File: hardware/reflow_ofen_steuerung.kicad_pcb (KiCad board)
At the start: 2 copper layers, 150.9 x 55.9 mm, 49 parts, among them J1 230VAC, J10 GND, J2 Heizung oben, J3 Heizung unten, J4 AVR-ISP-6, J5 LCD Display, J6 Encoder, J7 FAN, J8 +5V, J9 +12V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

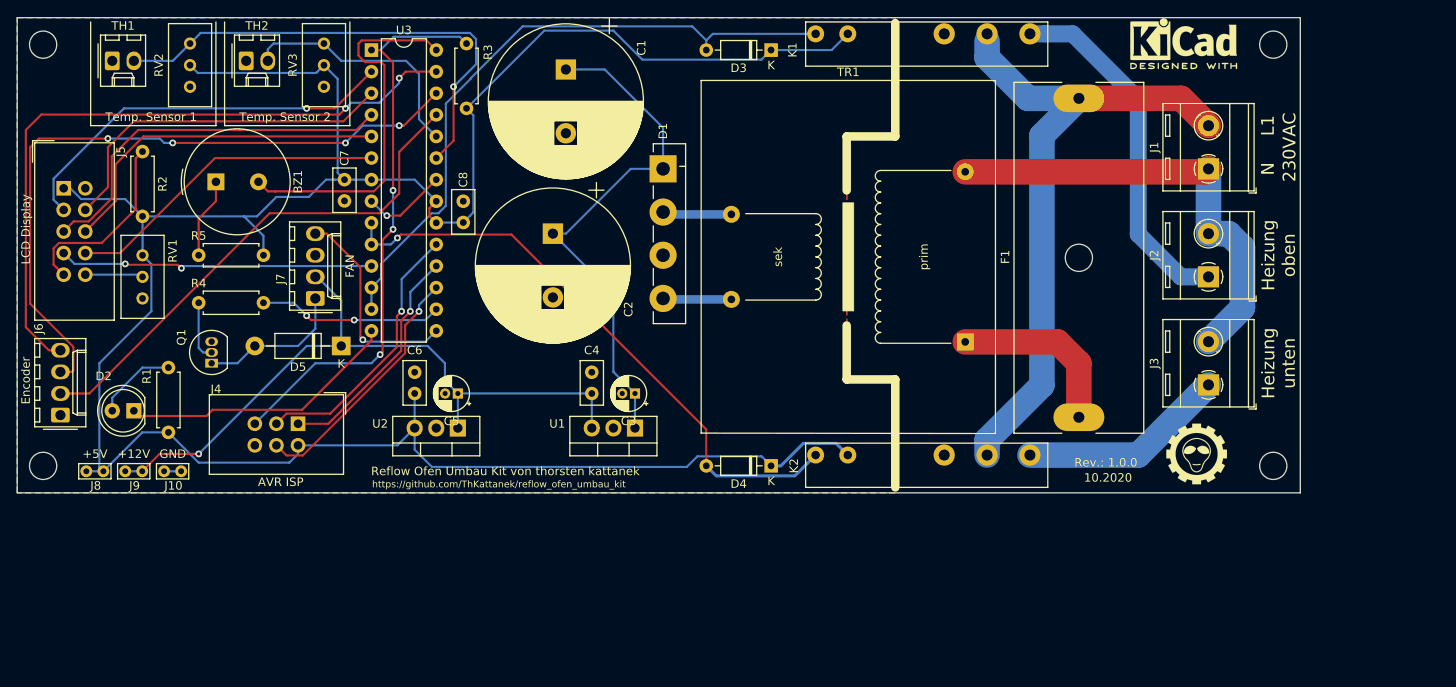
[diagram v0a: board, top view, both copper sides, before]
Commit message: changed label ADC0/1 to TEMP_SENSOR1/2
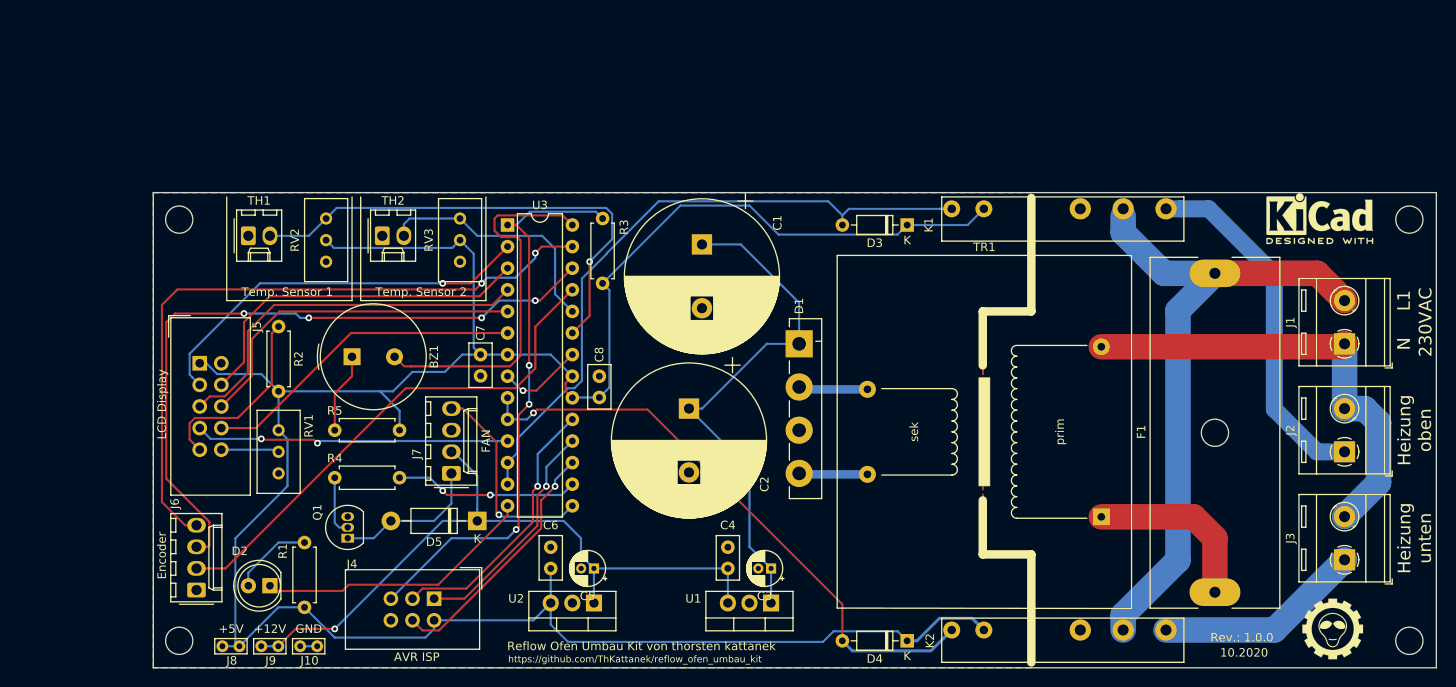
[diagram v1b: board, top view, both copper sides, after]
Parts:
- moved BZ1 26.1 mm to (91.7, 88.1)
- moved J5 26.1 mm to (73.8, 88.9)
- moved K2 26.1 mm to (182.4, 120.3)
- moved C1 26.1 mm to (132.8, 74.9)
- moved D3 26.1 mm to (157.0, 72.6)
- moved K1 26.1 mm to (182.4, 70.7)
- moved RV3 26.1 mm to (104.4, 71.9)
- moved C2 26.1 mm to (131.3, 94.2)
- moved C8 26.1 mm to (120.8, 90.4)
- moved D4 26.1 mm to (157.0, 121.5)
- moved F1 26.1 mm to (193.2, 115.8)
- moved J1 26.1 mm to (208.4, 86.6)
- moved J10 26.1 mm to (85.6, 122.2)
- moved J2 26.1 mm to (208.4, 99.3)
- moved J3 26.1 mm to (208.4, 112.0)
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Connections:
- net ADC0 renamed TEMP_SENSOR1
- net ADC1 renamed TEMP_SENSOR2

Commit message: Brückengleichrichter D1 korrigiert
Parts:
- D1: value B40C1500G -> B40C2300-1500A; footprint Diode_THT:Diode_Bridge_Vishay_GBL -> Diode_THT:Diode_Bridge_19.0x3.5x10.0mm_P5.0mm
- moved D1 17.5 mm to (144.8, 104.1), turned to 90 degrees
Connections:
- D1 pad 1: Net-(C1-Pad1) -> GND
- D1 pad 3: GND -> Net-(D1-Pad3)
- D1 pad 4: Net-(D1-Pad4) -> Net-(C1-Pad1)
- TR1 pad 7: Net-(D1-Pad2) -> Net-(D1-Pad3)
- TR1 pad 9: Net-(D1-Pad4) -> Net-(D1-Pad2)
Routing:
- net Net-(D1-Pad3): track 0.00 -> 8.42 mm
- net Net-(D1-Pad4): track 8.08 -> 0.00 mm
- net Net-(C1-Pad1): track 62.1 -> 60.1 mm
- net Net-(D1-Pad2): track 8.14 -> 8.69 mm
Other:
- board text added: "11.2020"
- board text added: "Rev.: 1.0.1"
- board text removed: "10.2020"
- board text removed: "Rev.: 1.0.0"
